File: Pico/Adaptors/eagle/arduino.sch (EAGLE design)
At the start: 3 parts

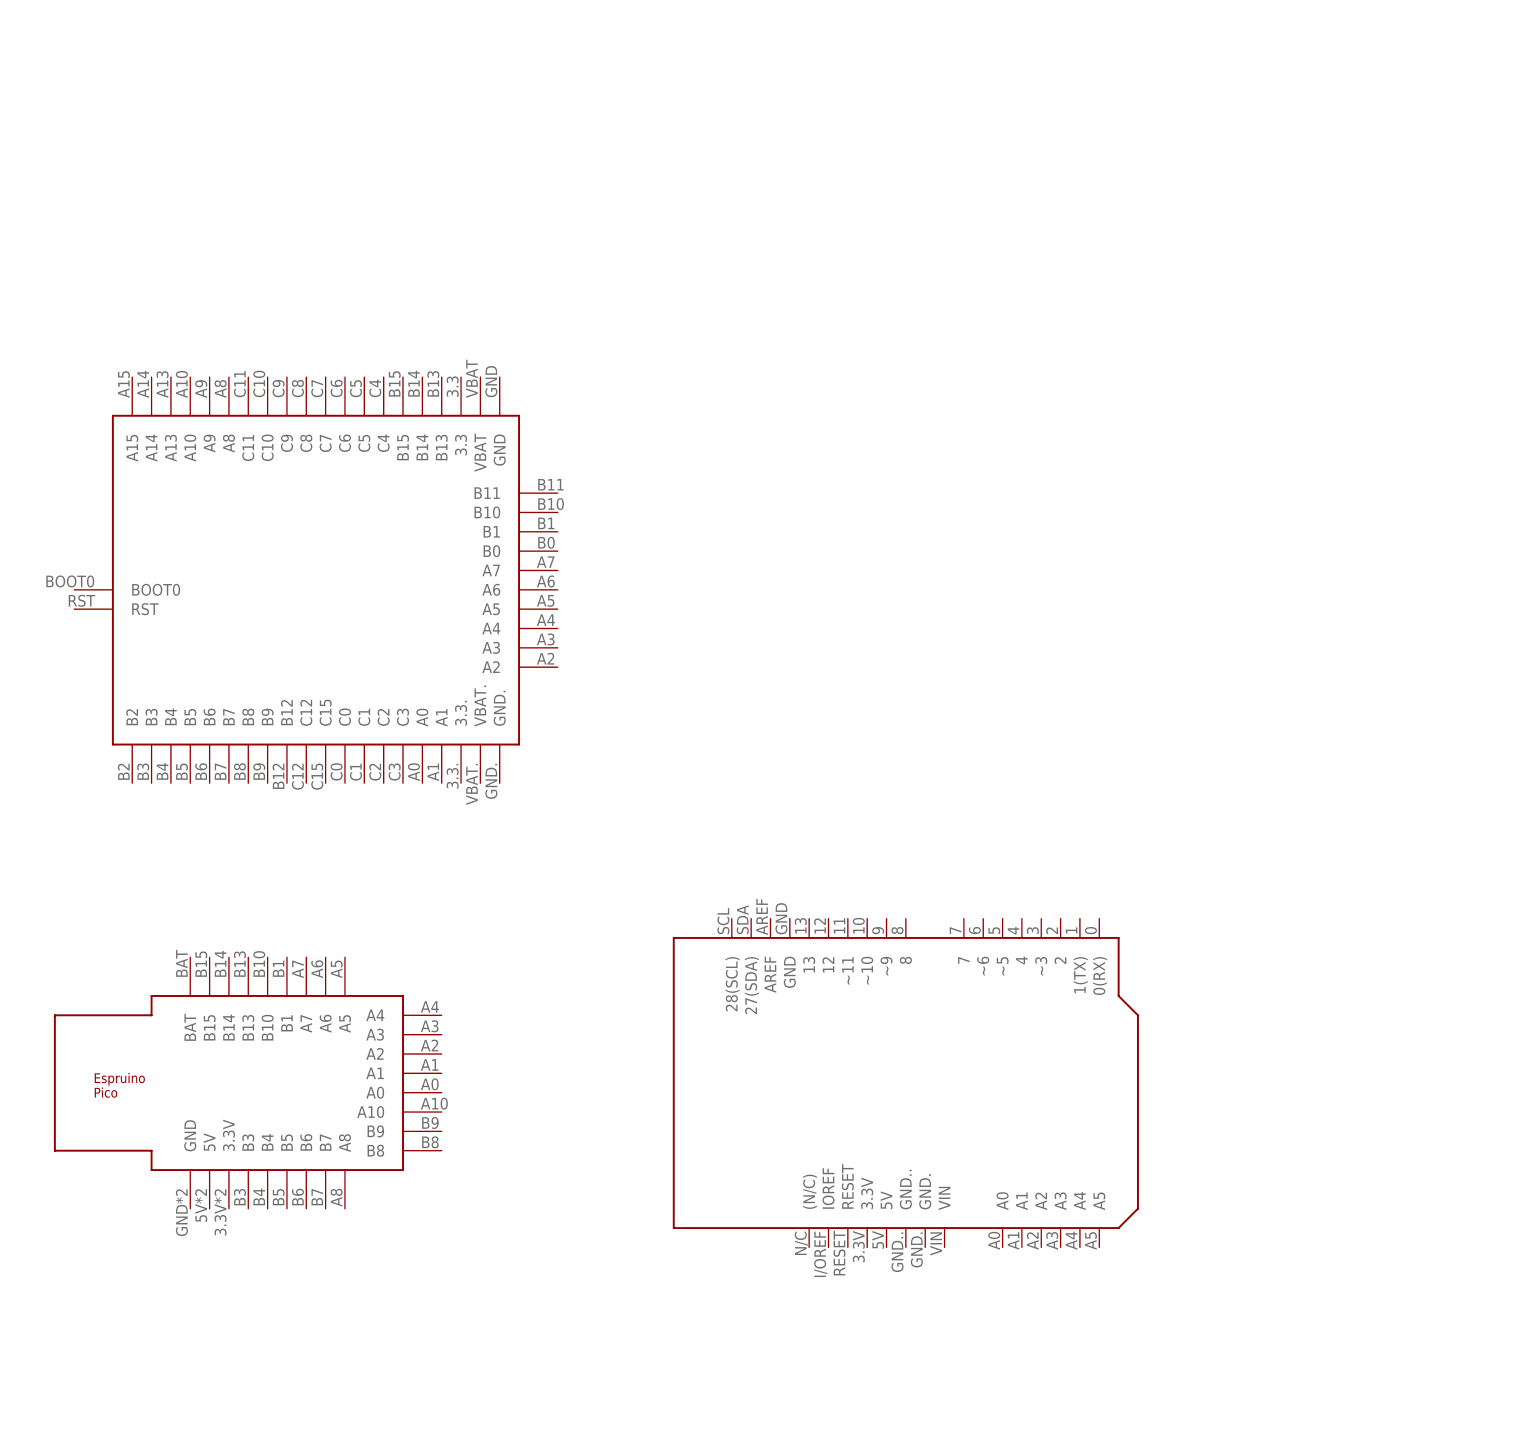
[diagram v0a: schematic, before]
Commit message: nrf24 adaptor, and DRC
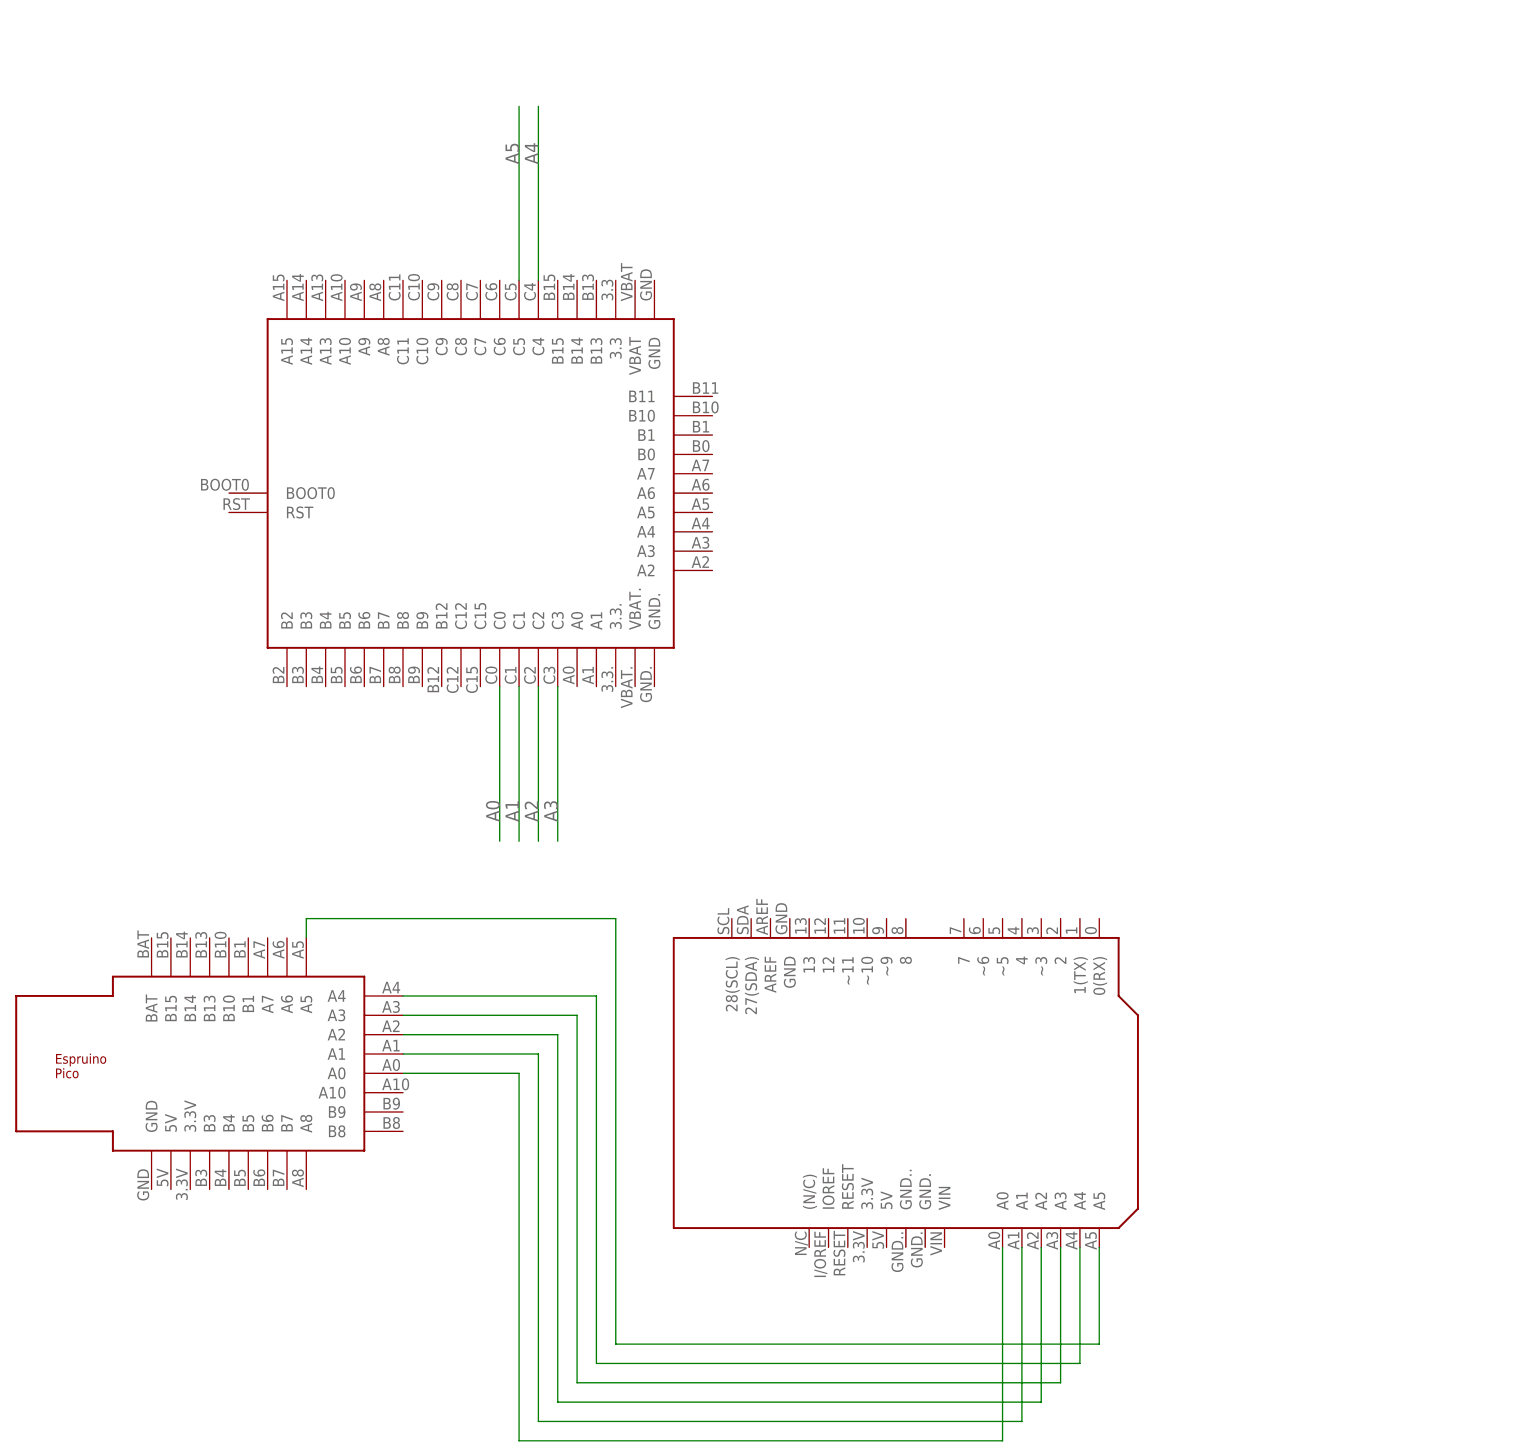
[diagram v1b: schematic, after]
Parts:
- U$1: value ESPRUINO_PICO_PIN -> ESPRUINO_PICO_SMDONLY; device espruino_pico:ESPRUINO_PICO_PIN -> espruino_pico:ESPRUINO_PICO_SMDONLY
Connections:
- new net A0: U$1.A0, U$2.A0, U$3.C0
- new net A1: U$1.A1, U$2.A1, U$3.C1
- new net A2: U$1.A2, U$2.A2, U$3.C2
- new net A3: U$1.A3, U$2.A3, U$3.C3
- new net A4: U$1.A4, U$2.A4, U$3.C4
- new net A5: U$1.A5, U$2.A5, U$3.C5
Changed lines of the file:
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@@
 </classes>
 <parts>
-<part name="U$1" library="espruino_pico" deviceset="ESPRUINO_PICO_PIN" device=""/>
 <part name="U$2" library="arduino" deviceset="ARDUINO" device=""/>
 <part name="U$3" library="espruino_pico" deviceset="ESPRUINO" device=""/>
+<part name="U$1" library="espruino_pico" deviceset="ESPRUINO_PICO_SMDONLY" device=""/>
 </parts>
 <sheets>
@@
 </plain>
 <instances>
-<instance part="U$1" gate="G$1" x="-2.54" y="40.64"/>
 <instance part="U$2" gate="G$1" x="86.36" y="33.02"/>
-<instance part="U$3" gate="G$1" x="2.54" y="106.68" rot="R90"/>
+<instance part="U$3" gate="G$1" x="22.86" y="119.38" rot="R90"/>
+<instance part="U$1" gate="G$1" x="-7.62" y="43.18"/>
 </instances>
 <busses>
 </busses>
 <nets>
+<net name="A0" class="0">
+<segment>
+<pinref part="U$3" gate="G$1" pin="C0"/>
+<wire x1="30.48" y1="83.82" x2="30.48" y2="63.5" width="0.1524" layer="91"/>
+<label x="30.48" y="66.04" size="1.778" layer="95" rot="R90"/>
+</segment>
+<segment>
+<pinref part="U$1" gate="G$1" pin="A0"/>
+<wire x1="17.78" y1="33.02" x2="33.02" y2="33.02" width="0.1524" layer="91"/>
+<wire x1="33.02" y1="33.02" x2="33.02" y2="-15.24" width="0.1524" layer="91"/>
+<pinref part="U$2" gate="G$1" pin="A0"/>
+<wire x1="33.02" y1="-15.24" x2="96.52" y2="-15.24" width="0.1524" layer="91"/>
+<wire x1="96.52" y1="-15.24" x2="96.52" y2="10.16" width="0.1524" layer="91"/>
+</segment>
+</net>
+<net name="A1" class="0">
+<segment>
+<pinref part="U$3" gate="G$1" pin="C1"/>
+<wire x1="33.02" y1="83.82" x2="33.02" y2="63.5" width="0.1524" layer="91"/>
+<label x="33.02" y="66.04" size="1.778" layer="95" rot="R90"/>
+</segment>
+<segment>
+<pinref part="U$2" gate="G$1" pin="A1"/>
+<wire x1="99.06" y1="10.16" x2="99.06" y2="-12.7" width="0.1524" layer="91"/>
+<wire x1="99.06" y1="-12.7" x2="35.56" y2="-12.7" width="0.1524" layer="91"/>
+<wire x1="35.56" y1="-12.7" x2="35.56" y2="35.56" width="0.1524" layer="91"/>
+<pinref part="U$1" gate="G$1" pin="A1"/>
+<wire x1="35.56" y1="35.56" x2="17.78" y2="35.56" width="0.1524" layer="91"/>
+</segment>
+</net>
+<net name="A2" class="0">
+<segment>
+<pinref part="U$3" gate="G$1" pin="C2"/>
+<wire x1="35.56" y1="83.82" x2="35.56" y2="63.5" width="0.1524" layer="91"/>
+<label x="35.56" y="66.04" size="1.778" layer="95" rot="R90"/>
+</segment>
+<segment>
+<pinref part="U$1" gate="G$1" pin="A2"/>
+<wire x1="17.78" y1="38.1" x2="38.1" y2="38.1" width="0.1524" layer="91"/>
+<wire x1="38.1" y1="38.1" x2="38.1" y2="-10.16" width="0.1524" layer="91"/>
+<wire x1="38.1" y1="-10.16" x2="101.6" y2="-10.16" width="0.1524" layer="91"/>
+<pinref part="U$2" gate="G$1" pin="A2"/>
+<wire x1="101.6" y1="-10.16" x2="101.6" y2="10.16" width="0.1524" layer="91"/>
+</segment>
+</net>
+<net name="A3" class="0">
+<segment>
+<pinref part="U$3" gate="G$1" pin="C3"/>
+<wire x1="38.1" y1="83.82" x2="38.1" y2="63.5" width="0.1524" layer="91"/>
+<label x="38.1" y="66.04" size="1.778" layer="95" rot="R90"/>
+</segment>
+<segment>
+<pinref part="U$2" gate="G$1" pin="A3"/>
+<wire x1="104.14" y1="10.16" x2="104.14" y2="-7.62" width="0.1524" layer="91"/>
+<wire x1="104.14" y1="-7.62" x2="40.64" y2="-7.62" width="0.1524" layer="91"/>
+<wire x1="40.64" y1="-7.62" x2="40.64" y2="40.64" width="0.1524" layer="91"/>
+<pinref part="U$1" gate="G$1" pin="A3"/>
+<wire x1="40.64" y1="40.64" x2="17.78" y2="40.64" width="0.1524" layer="91"/>
+</segment>
+</net>
+<net name="A4" class="0">
+<segment>
+<pinref part="U$3" gate="G$1" pin="C4"/>
+<wire x1="35.56" y1="137.16" x2="35.56" y2="160.02" width="0.1524" layer="91"/>
+<label x="35.56" y="152.4" size="1.778" layer="95" rot="R90"/>
+</segment>
+<segment>
+<pinref part="U$1" gate="G$1" pin="A4"/>
+<wire x1="17.78" y1="43.18" x2="43.18" y2="43.18" width="0.1524" layer="91"/>
+<wire x1="43.18" y1="43.18" x2="43.18" y2="-5.08" width="0.1524" layer="91"/>
+<wire x1="43.18" y1="-5.08" x2="106.68" y2="-5.08" width="0.1524" layer="91"/>
+<pinref part="U$2" gate="G$1" pin="A4"/>
+<wire x1="106.68" y1="-5.08" x2="106.68" y2="10.16" width="0.1524" layer="91"/>
+</segment>
+</net>
+<net name="A5" class="0">
+<segment>
+<pinref part="U$3" gate="G$1" pin="C5"/>
+<wire x1="33.02" y1="137.16" x2="33.02" y2="160.02" width="0.1524" layer="91"/>
+<label x="33.02" y="152.4" size="1.778" layer="95" rot="R90"/>
+</segment>
+<segment>
+<pinref part="U$2" gate="G$1" pin="A5"/>
+<wire x1="109.22" y1="10.16" x2="109.22" y2="-2.54" width="0.1524" layer="91"/>
+<wire x1="109.22" y1="-2.54" x2="45.72" y2="-2.54" width="0.1524" layer="91"/>
+<wire x1="45.72" y1="-2.54" x2="45.72" y2="53.34" width="0.1524" layer="91"/>
+<pinref part="U$1" gate="G$1" pin="A5"/>
+<wire x1="45.72" y1="53.34" x2="5.08" y2="53.34" width="0.1524" layer="91"/>
+<wire x1="5.08" y1="53.34" x2="5.08" y2="50.8" width="0.1524" layer="91"/>
+</segment>
+</net>
 </nets>
 </sheet>

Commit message: arduino adaptor
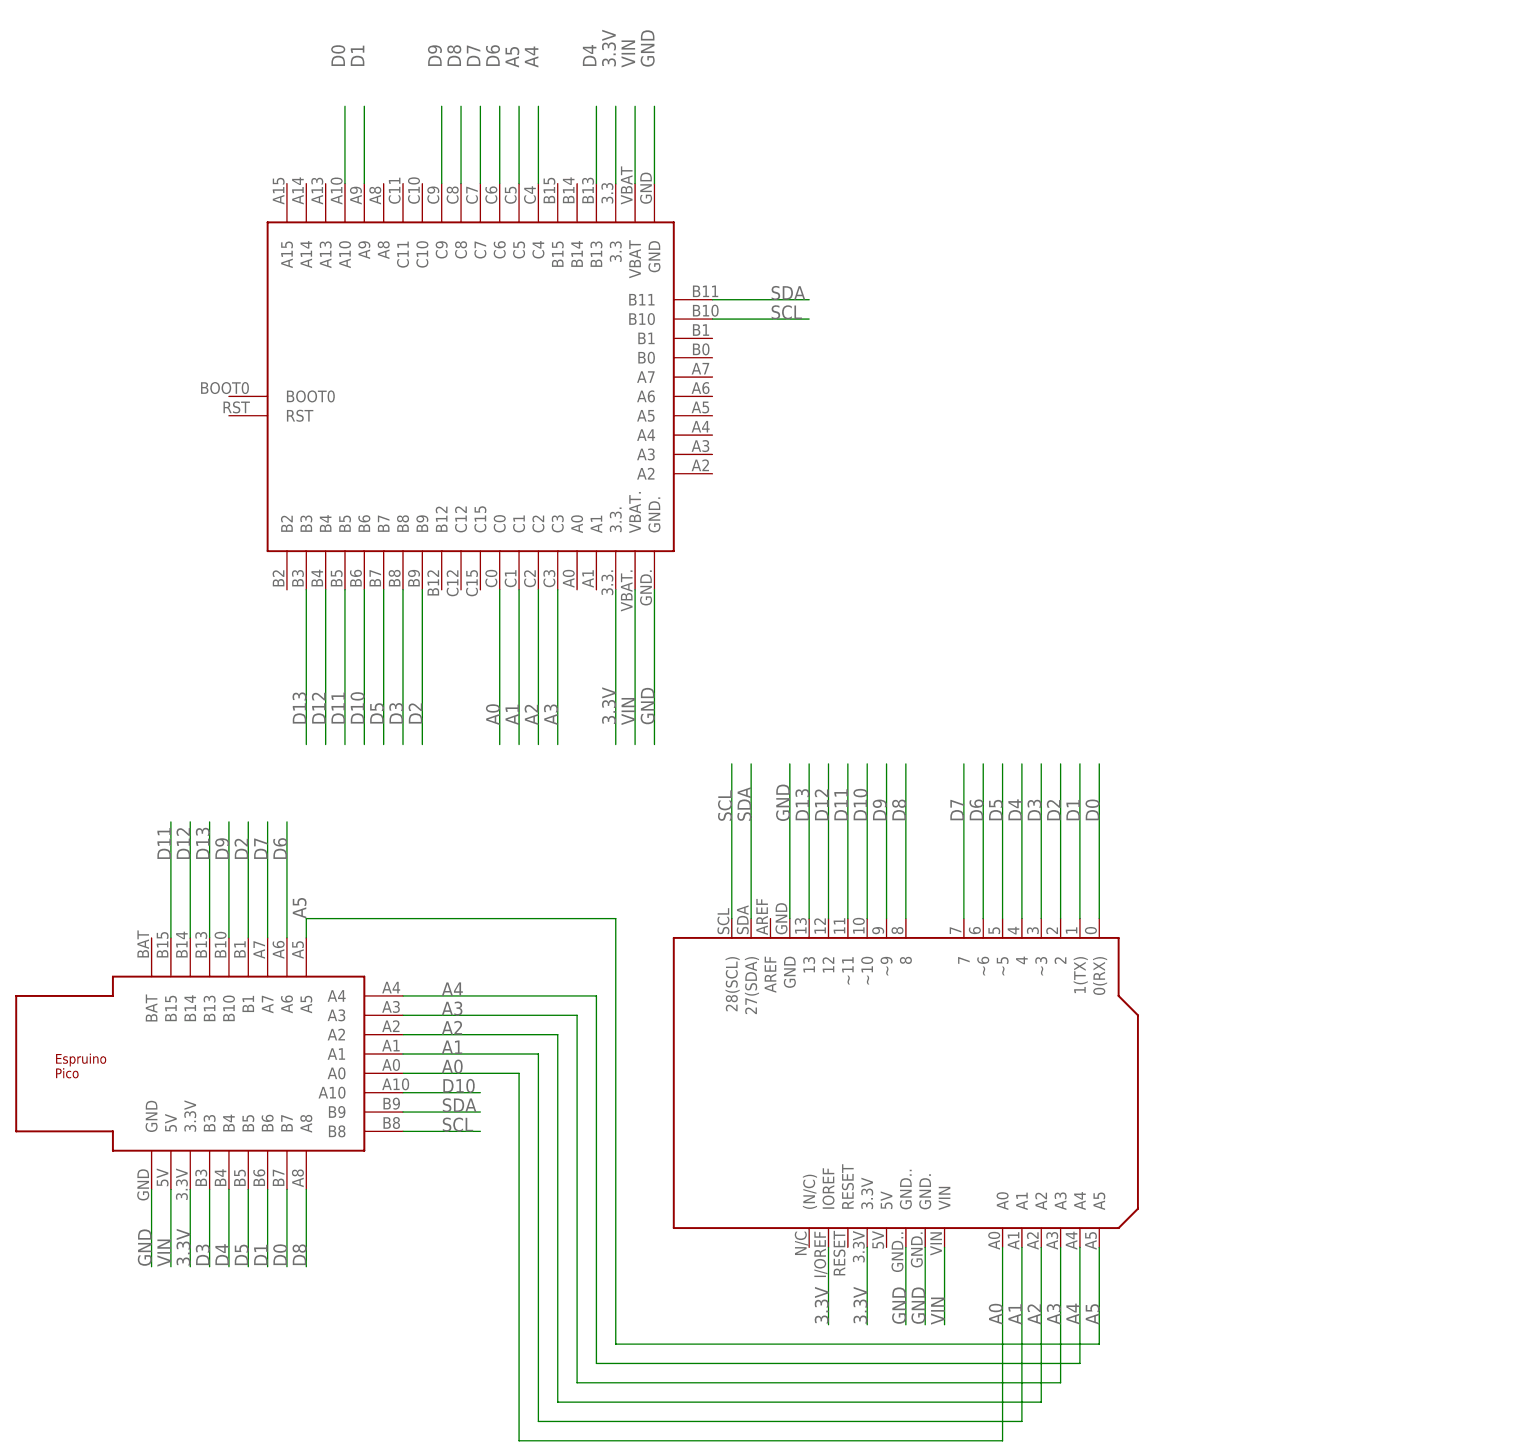
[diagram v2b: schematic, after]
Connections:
- new net 3.3V: U$1.3.3V, U$2.3.3V, U$2.IOREF, U$3.3.3, U$3.3.3.
- new net D0: U$1.B7, U$2.0(RX), U$3.A10
- new net D1: U$1.B6, U$2.1(TX), U$3.A9
- new net D10: U$1.A10, U$2.~10, U$3.B6
- new net D11: U$1.B15, U$2.~11, U$3.B5
- new net D12: U$1.B14, U$2.12, U$3.B4
- new net D13: U$1.B13, U$2.13, U$3.B3
- new net D2: U$1.B1, U$2.2, U$3.B9
- new net D3: U$1.B3, U$2.~3, U$3.B8
- new net D4: U$1.B4, U$2.4, U$3.B13
- new net D5: U$1.B5, U$2.~5, U$3.B7
- new net D6: U$1.A6, U$2.~6, U$3.C6
- new net D7: U$1.A7, U$2.7, U$3.C7
- new net D8: U$1.A8, U$2.8, U$3.C8
- new net D9: U$1.B10, U$2.~9, U$3.C9
- new net GND: U$1.GND, U$2.GND, U$2.GND., U$2.GND.., U$3.GND, U$3.GND.
- new net SCL: U$1.B8, U$2.28(SCL), U$3.B10
- new net SDA: U$1.B9, U$2.27(SDA), U$3.B11
- new net VIN: U$1.5V, U$2.VIN, U$3.VBAT, U$3.VBAT.

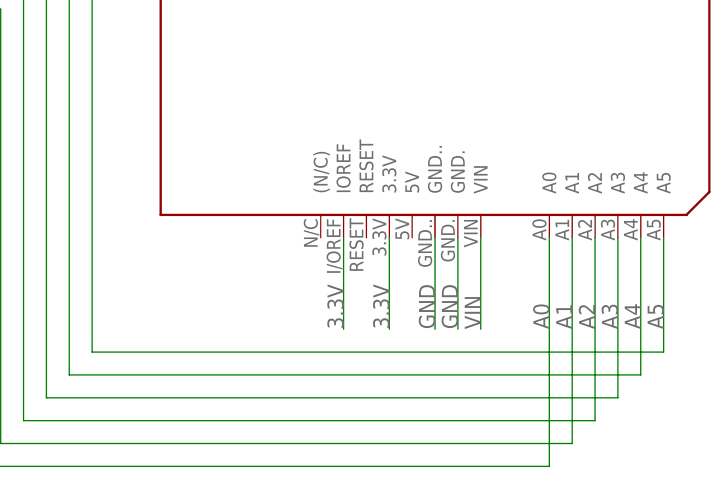
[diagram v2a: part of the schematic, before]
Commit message: connect Vin and 5V, allowing shields to be powered from USB volts
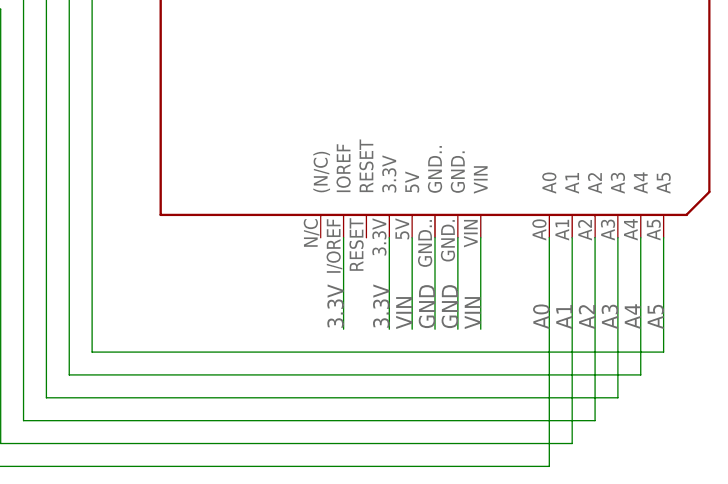
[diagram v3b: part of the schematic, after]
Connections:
- net VIN: now also U$2.5V
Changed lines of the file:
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@@
 <label x="-12.7" y="7.62" size="1.778" layer="95" rot="R90"/>
+</segment>
+<segment>
+<pinref part="U$2" gate="G$1" pin="5V"/>
+<wire x1="81.28" y1="10.16" x2="81.28" y2="0" width="0.1524" layer="91"/>
+<label x="81.28" y="0" size="1.778" layer="95" rot="R90"/>
 </segment>
 </net>
